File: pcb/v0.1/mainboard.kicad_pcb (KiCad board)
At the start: 4 copper layers, 156.4 x 94.8 mm, 124 parts, among them J1 Conn_01x02_Pin, J11 Conn_01x03_Pin, J12 Conn_02x08_Odd_Even, J13 Conn_02x08_Odd_Even, J2 TYPE_C_Receptacle, J3 Conn_01x04_Pin, J4 TYPE_C_Receptacle, J5 TYPE_C_Receptacle, J6 22s_disp_connector, J7 ComputeModule5-CM5_connector, J8 Micro_SD_molex, J9 AudioJack3, Q1 MMBT2222A, SW1 SW_Push_45deg, U1 AP2112K-3.3TRG1, U2 Nexperia PUSB3FR4Z, U3 Nexperia PUSB3FR4Z, U4 PCM5102A, U5 RT9742GGJ5, U6 RT9742GGJ5, U7 MDBT50Q-P1MV2, U8 AP22653W6-7, Y1 O_32.768kHz

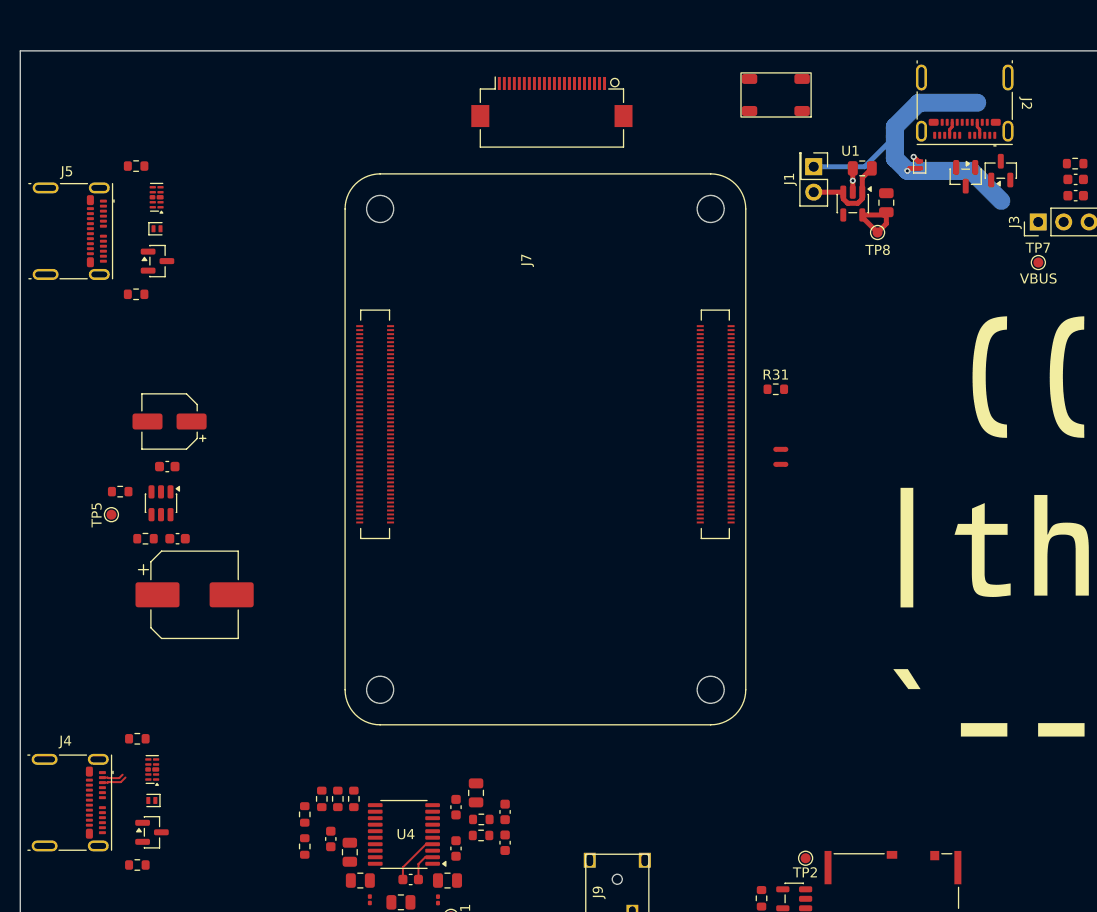
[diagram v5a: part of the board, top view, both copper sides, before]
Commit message: Remove USB Type-c ports + minor changes + dru file
The current USB type-c ports aren't properly routable without using via
in pad, which at the current stage is prohibitively expensive. I've
removed them for now with the intent of swapping them out for ones from
GTC.

Additionally I noticed that a dru file has not been committed this whole
time. Its existed for a while on my computer.
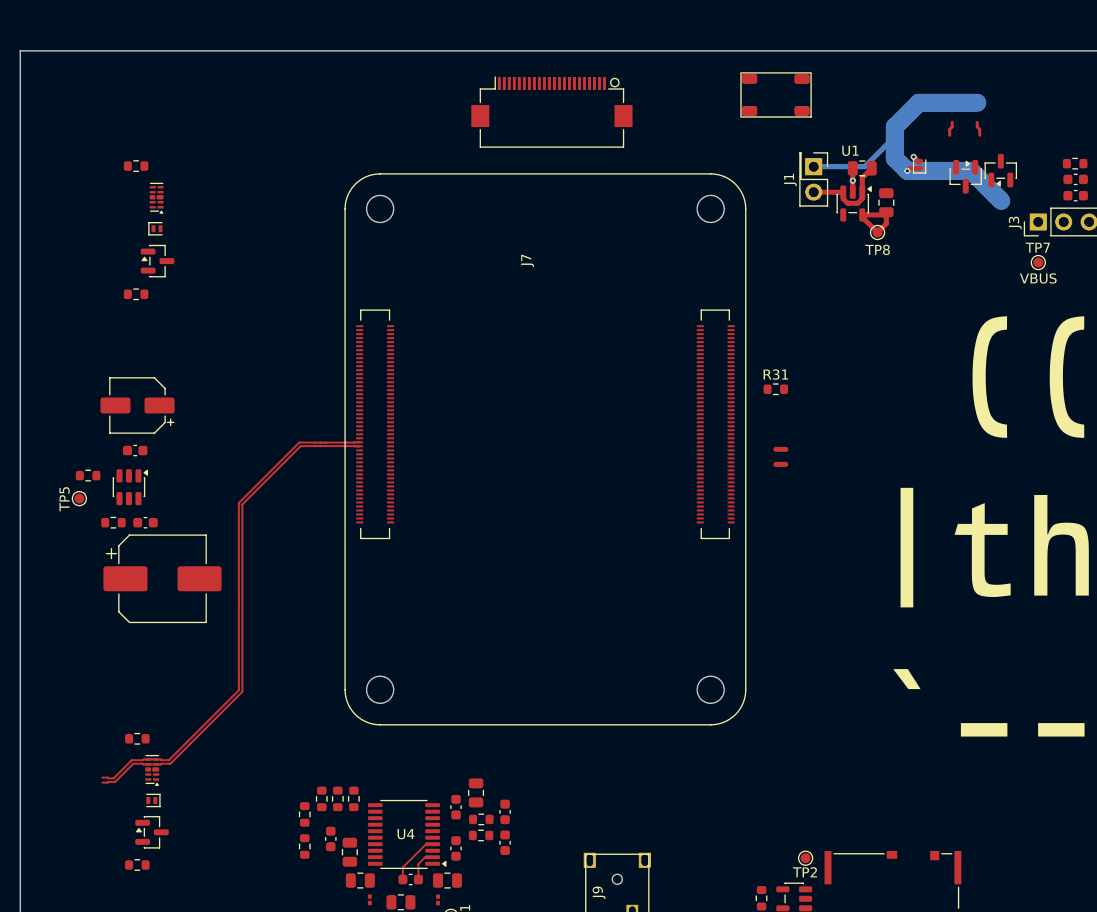
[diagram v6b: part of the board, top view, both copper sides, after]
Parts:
- removed J2, J4, J5: TYPE_C_Receptacle, Connector_USB:USB_C_Receptacle_Molex_105450-0101
- moved R19 3.58 mm to (32.9, 78.6)
- moved C30 3.58 mm to (35.3, 66.9)
- moved C33 3.58 mm to (37.8, 84.2)
- moved R18 3.58 mm to (30.4, 73.9)
- moved TP5 3.58 mm to (29.5, 76.2)
- moved C32 3.58 mm to (36.1, 78.6)
- moved C31 3.58 mm to (35.1, 71.4)
- moved U8 3.58 mm to (34.5, 75.1)
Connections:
- U2 pad 10: unconnected-(U2-NC-Pad10) -> /HighSpeed/USB3-0-RX_N
- U2 pad 6: unconnected-(U2-NC-Pad6) -> /HighSpeed/USB3-0-TX_P
- U2 pad 7: unconnected-(U2-NC-Pad7) -> /HighSpeed/USB3-0-TX_N
- U2 pad 9: unconnected-(U2-NC-Pad9) -> /HighSpeed/USB3-0-RX_P
- U3 pad 10: unconnected-(U3-NC-Pad10) -> /HighSpeed/USB3-1-RX_N
- U3 pad 6: unconnected-(U3-NC-Pad6) -> /HighSpeed/USB3-1-TX_P
- U3 pad 7: unconnected-(U3-NC-Pad7) -> /HighSpeed/USB3-1-TX_N
- U3 pad 9: unconnected-(U3-NC-Pad9) -> /HighSpeed/USB3-1-RX_P
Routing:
- net /HighSpeed/USB3-0-TX_P: track 2.18 -> 50.6 mm
- net /HighSpeed/USB3-0-TX_N: track 2.51 -> 50.6 mm

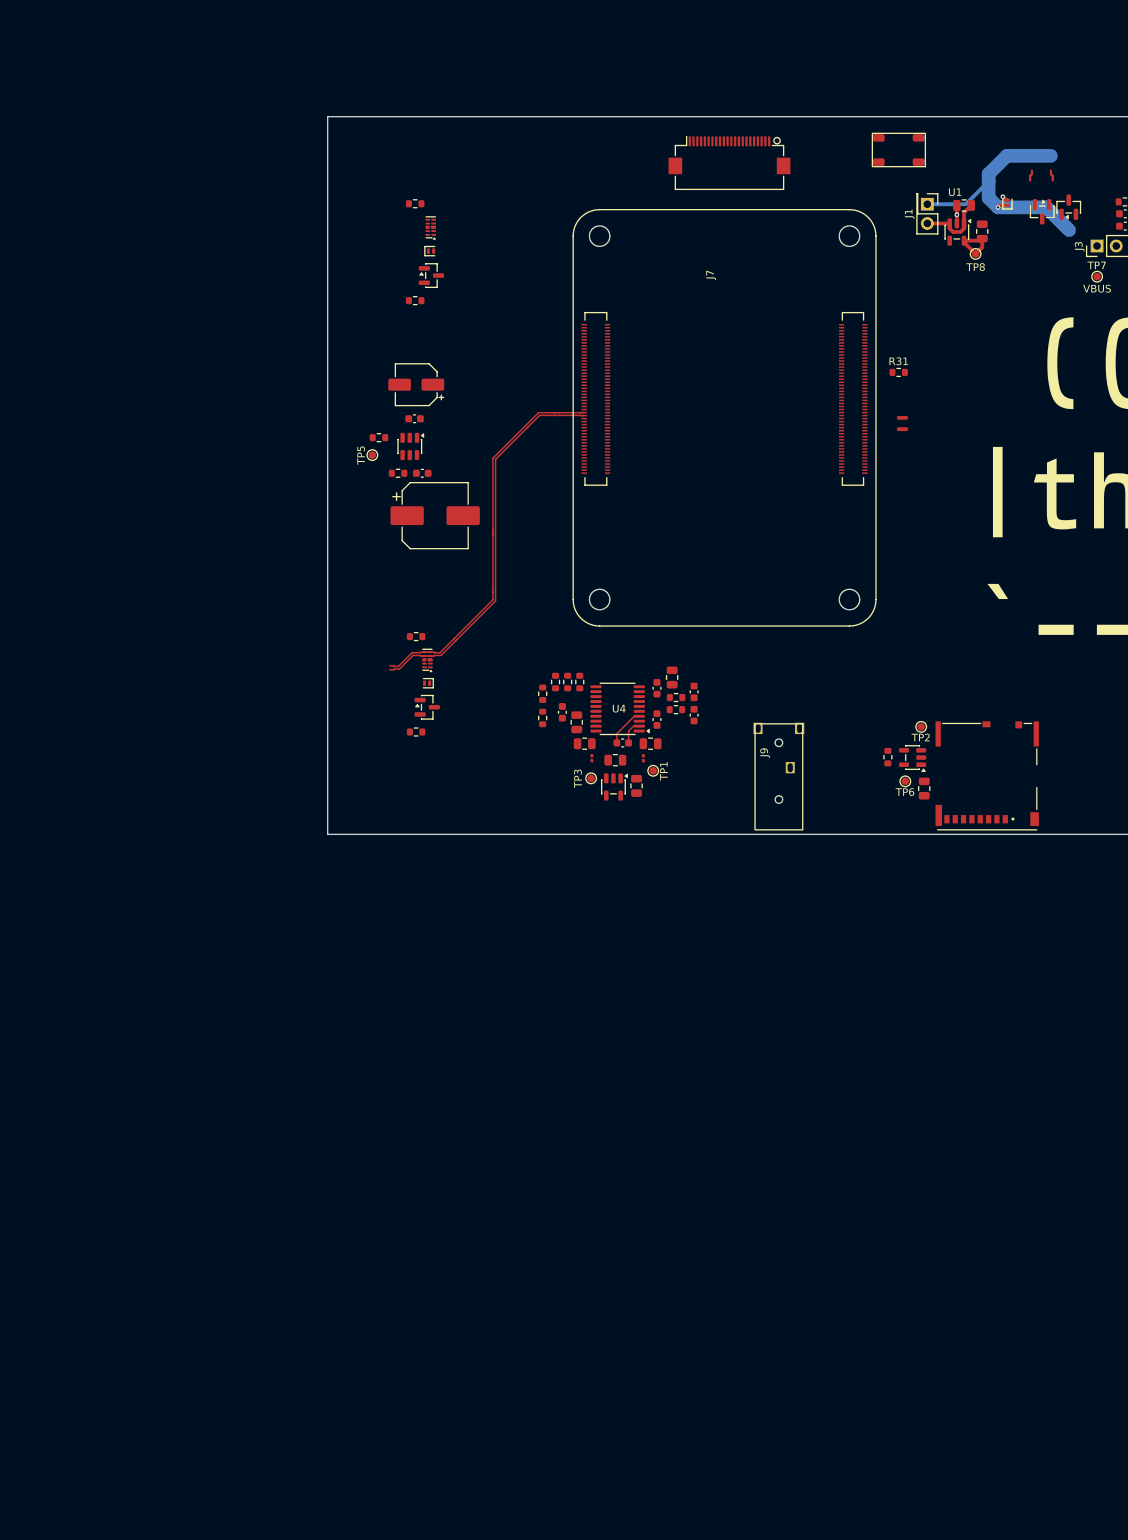
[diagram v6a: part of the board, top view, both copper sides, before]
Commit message: USB differential pairs complete.
Had to break these out from the rest of the pcb as they just didn't add
up otherwise. Will continue to do the high speed lines separately before
re assembling the pcb.
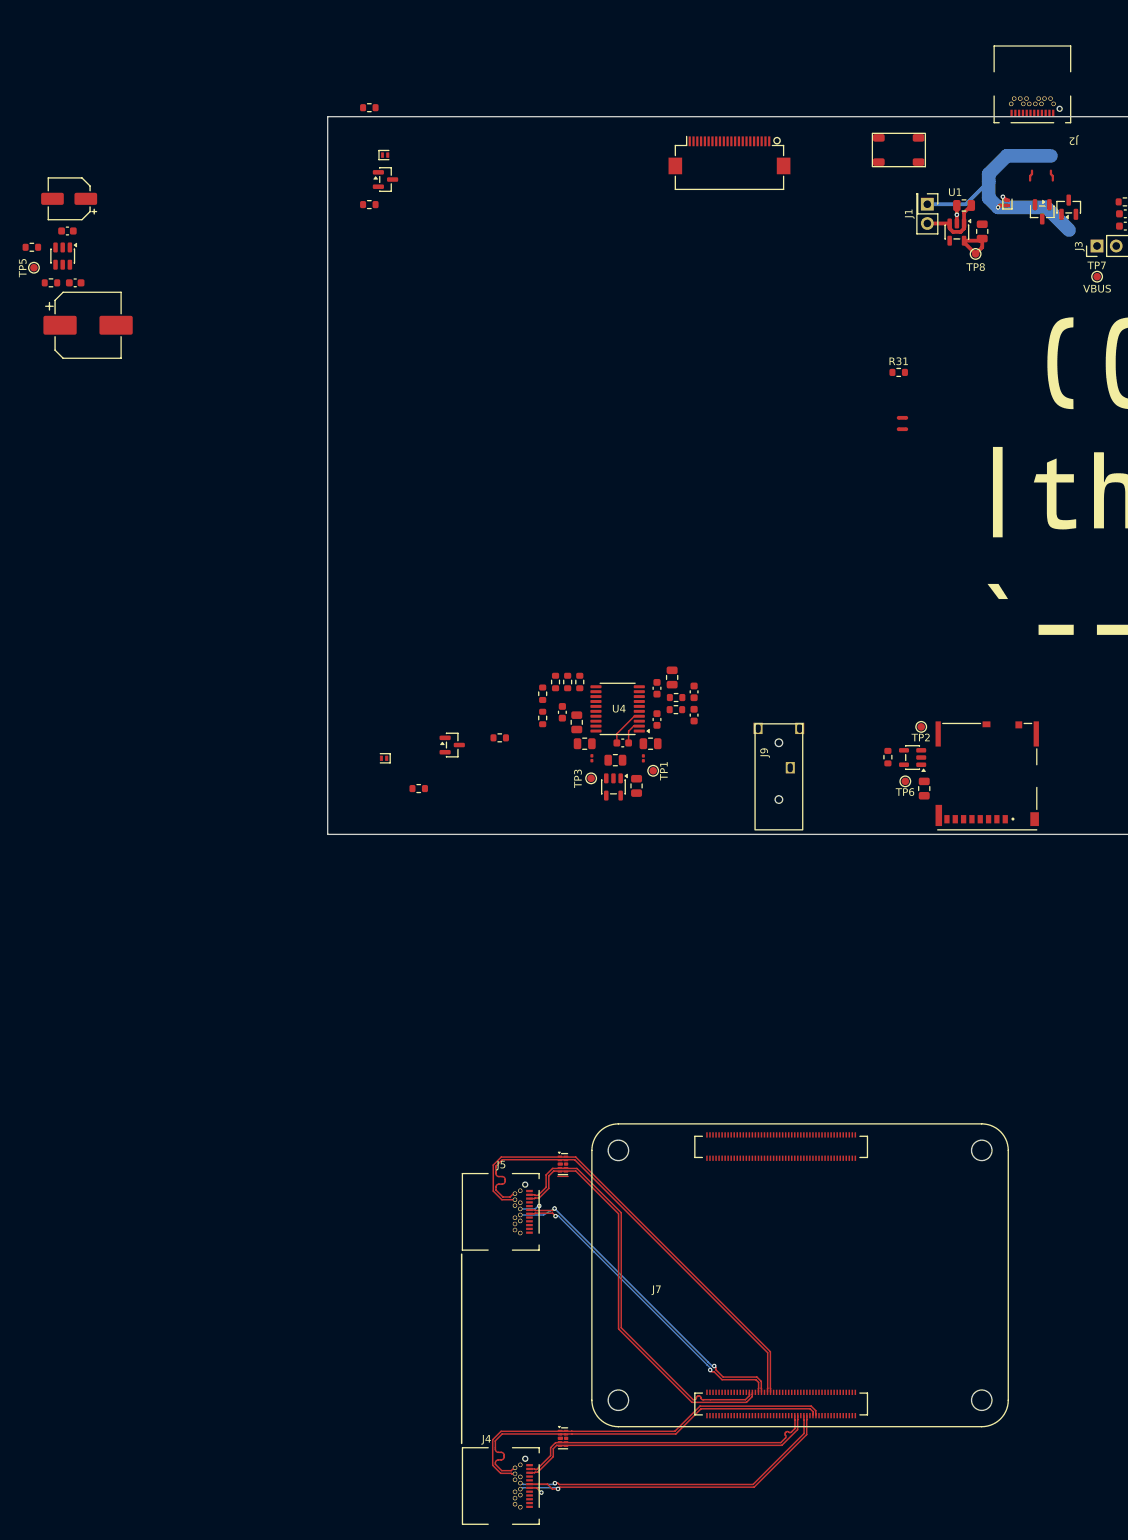
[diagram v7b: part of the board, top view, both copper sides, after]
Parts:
- added J2: TYPE_C_Receptacle, TH-1-CC_footprints:USB4056-03-A, F.Cu at (122.1, 34.2)
- added J4: TYPE_C_Receptacle, TH-1-CC_footprints:USB4056-03-A, F.Cu at (53.4, 206.9)
- added J5: TYPE_C_Receptacle, TH-1-CC_footprints:USB4056-03-A, F.Cu at (53.4, 170.7)
- moved U3 125.0 mm to (54.7, 169.8), turned to 0 degrees
- moved J7 124.6 mm to (62.0, 168.0), turned to -90 degrees
- moved U2 104.4 mm to (54.7, 206.1), turned to 0 degrees
- moved C32 52.3 mm to (-9.75, 53.5)
- moved R18 52.3 mm to (-15.5, 48.8)
- moved U8 52.3 mm to (-11.4, 49.9)
- moved C33 52.3 mm to (-8.05, 59.0)
- moved R19 52.3 mm to (-12.9, 53.5)
- moved C31 52.1 mm to (-10.8, 46.6)
- moved C30 52.0 mm to (-10.6, 42.4)
- moved TP5 51.1 mm to (-15.2, 51.5)
- moved R23 17.3 mm to (46.3, 113.5)
- moved D25 14.1 mm to (31.2, 36.6)
- moved D3 14.1 mm to (31.2, 39.8)
- moved R20 14.1 mm to (29.1, 30.3)
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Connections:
- U2 pad 4: /HighSpeed/USB3-0-TX_N -> /HighSpeed/USB3-0-TX_P
- U2 pad 5: /HighSpeed/USB3-0-TX_P -> /HighSpeed/USB3-0-TX_N
- U2 pad 6: /HighSpeed/USB3-0-TX_P -> /HighSpeed/USB3-0-TX_N
- U2 pad 7: /HighSpeed/USB3-0-TX_N -> /HighSpeed/USB3-0-TX_P
- U3 pad 4: /HighSpeed/USB3-1-TX_N -> /HighSpeed/USB3-1-TX_P
- U3 pad 5: /HighSpeed/USB3-1-TX_P -> /HighSpeed/USB3-1-TX_N
- U3 pad 6: /HighSpeed/USB3-1-TX_P -> /HighSpeed/USB3-1-TX_N
- U3 pad 7: /HighSpeed/USB3-1-TX_N -> /HighSpeed/USB3-1-TX_P
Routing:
- net /HighSpeed/USB3-1-RX_N: track 0.00 -> 59.8 mm
- net /HighSpeed/USB3-1-RX_P: track 0.00 -> 59.8 mm
- net /HighSpeed/USB3-1-TX_N: track 0.00 -> 54.3 mm
- net /HighSpeed/USB3-1-TX_P: track 0.00 -> 54.3 mm
- net /HighSpeed/USB3-0-RX_N: track 0.00 -> 52.6 mm
- net /HighSpeed/USB3-0-RX_P: track 0.00 -> 52.6 mm
- net /HighSpeed/USB3-0-D_P: track 0.00 -> 47.5 mm, vias 0 -> 1
- net /HighSpeed/USB3-0-D_N: track 0.00 -> 47.0 mm, vias 0 -> 2
- net /HighSpeed/USB3-1-D_P: track 0.00 -> 46.6 mm, vias 0 -> 2
- net /HighSpeed/USB3-1-D_N: track 0.00 -> 46.4 mm, vias 0 -> 3
- net /HighSpeed/USB3-0-TX_P: track 50.6 -> 40.7 mm
- net /HighSpeed/USB3-0-TX_N: track 50.6 -> 40.7 mm

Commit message: Finally out of high speed hell
Finished routing the differential pairs for the MIPI D-PHY connector.
With that all high speed lines are completed.
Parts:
- moved C1 242.9 mm to (-107.5, 156.1)
- moved C12 242.9 mm to (-157.6, 227.2)
- moved C13 242.9 mm to (-112.7, 233.1)
- moved C14 242.9 mm to (-148.9, 227.2)
- moved C17 242.9 mm to (-152.5, 227.1)
- moved C2 242.9 mm to (-105.1, 159.5)
- moved C20 242.9 mm to (-158.6, 224.3)
- moved C21 242.9 mm to (-143.1, 223.4)
- moved C22 242.9 mm to (-143.1, 220.3)
- moved C23 242.9 mm to (-150.7, 232.7)
- moved C24 242.9 mm to (-50.7, 198.0)
- moved C26 242.9 mm to (-52.0, 194.1)
- moved C27 242.9 mm to (-50.1, 190.8)
- moved C29 242.9 mm to (-77.1, 232.3)
- moved C3 242.9 mm to (-86.2, 158.8)
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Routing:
- net /HighSpeed/DPHY0_D0_P: track 0.00 -> 56.2 mm
- net /HighSpeed/DPHY0_D0_N: track 0.00 -> 56.2 mm
- net /HighSpeed/DPHY0_D1_P: track 0.00 -> 56.0 mm
- net /HighSpeed/DPHY0_D1_N: track 0.00 -> 56.0 mm
- net /HighSpeed/DPHY0_C_P: track 0.00 -> 55.9 mm
- net /HighSpeed/DPHY0_C_N: track 0.00 -> 55.9 mm
- net /HighSpeed/DPHY0_D2_N: track 0.00 -> 55.8 mm
- net /HighSpeed/DPHY0_D2_P: track 0.00 -> 55.8 mm
- net /HighSpeed/DPHY0_D3_N: track 0.00 -> 55.7 mm
- net /HighSpeed/DPHY0_D3_P: track 0.00 -> 55.7 mm
